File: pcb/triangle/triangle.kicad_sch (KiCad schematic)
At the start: 65 parts, among them J1 Conn_01x03_Male, J2 Conn_01x03_Male

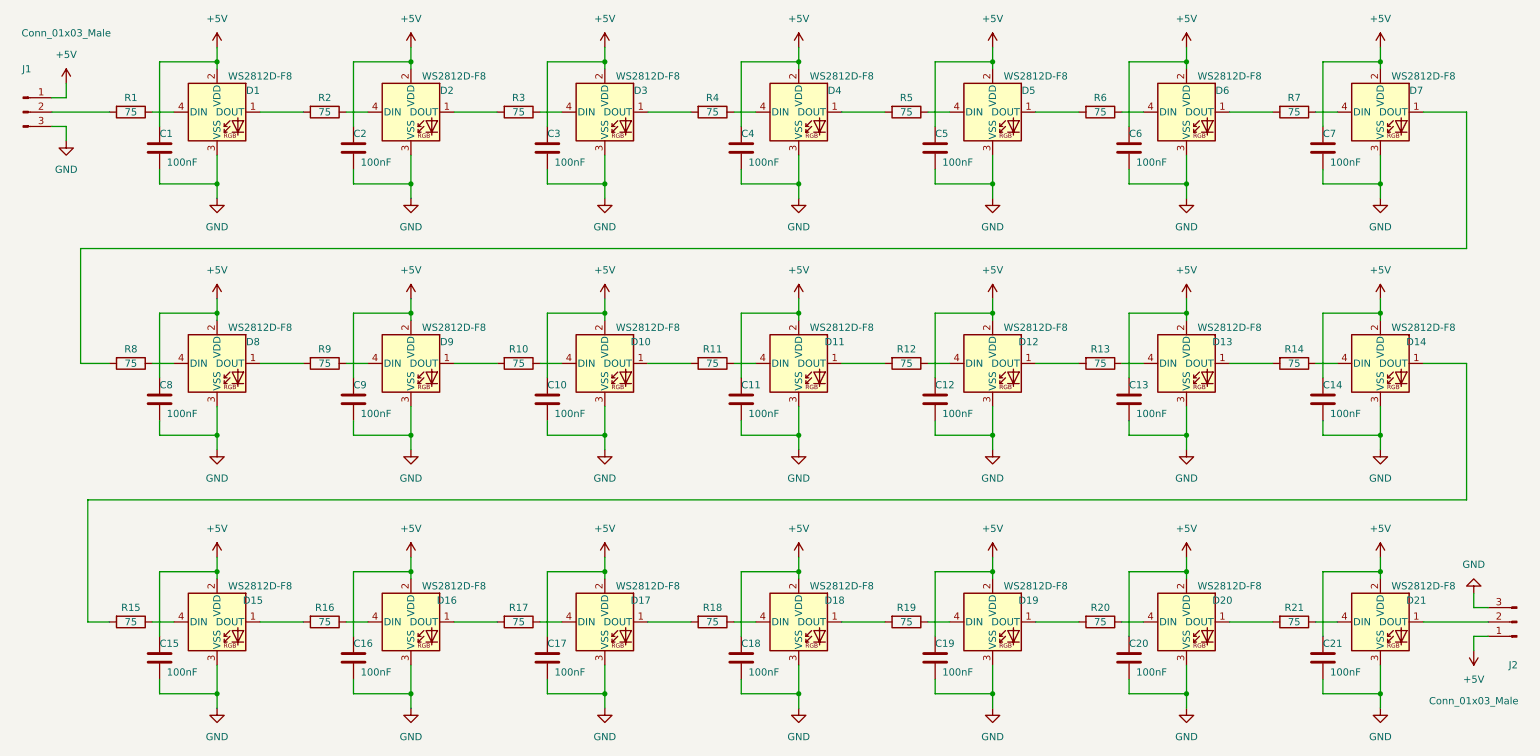
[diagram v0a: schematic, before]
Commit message: Split PCB one large PCB gap into 2 smaller gaps.
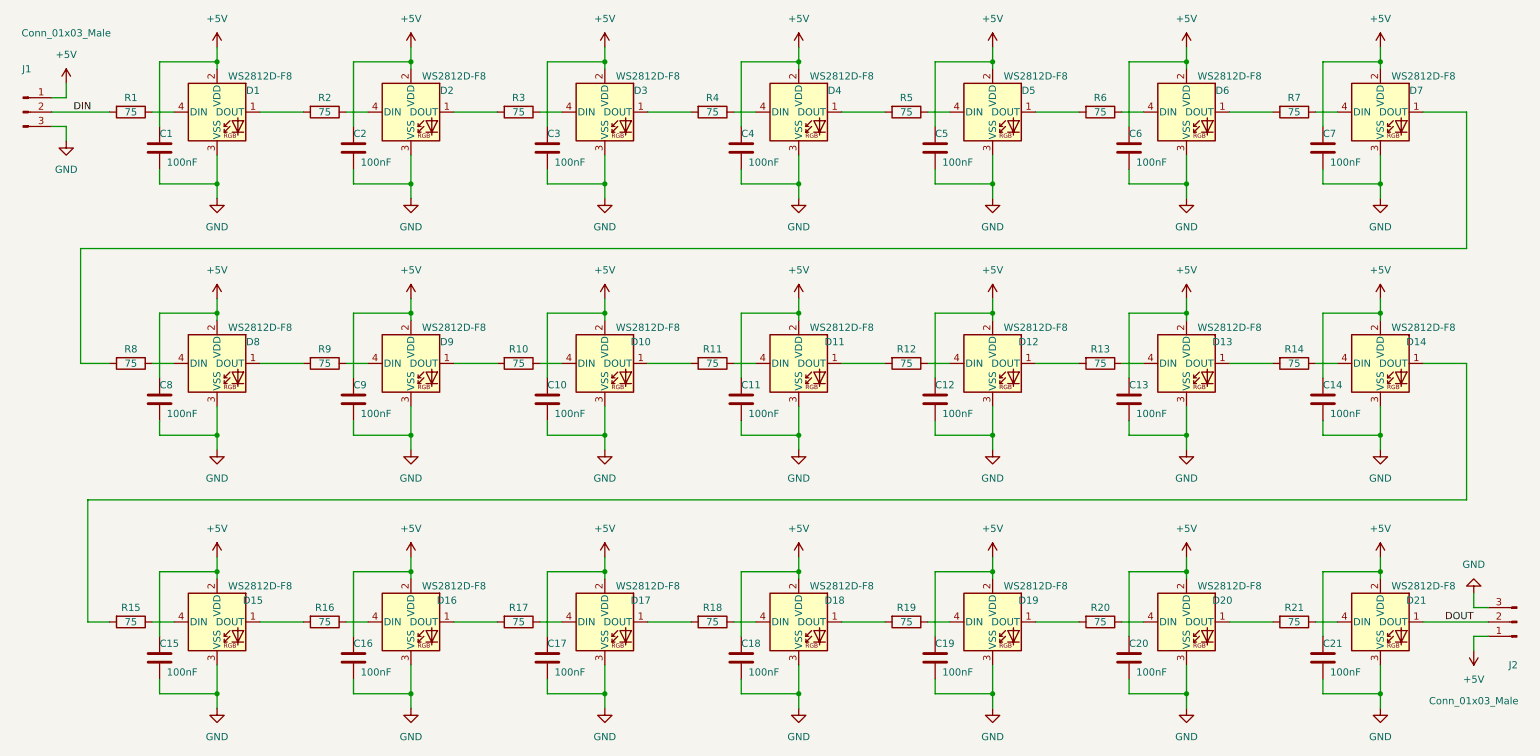
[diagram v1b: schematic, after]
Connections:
- net DIN: now reaches J1.2 (Pin_2), R1.2
- net DOUT: now reaches D21.1 (DOUT), J2.2 (Pin_2)
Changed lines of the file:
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@@
     (stroke (width 0) (type default) (color 0 0 0 0))
+  )
+  (label "DOUT" (at 265.43 138.43 0)
+    (effects (font (size 1.27 1.27)) (justify left bottom))
+  )
+  (label "DIN" (at 22.86 48.26 0)
+    (effects (font (size 1.27 1.27)) (justify left bottom))
   )
   (symbol (lib_id "Device:C") (at 106.68 54.61 0) (unit 1)
